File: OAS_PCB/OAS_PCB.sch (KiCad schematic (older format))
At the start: 57 parts, among them U1 TL072

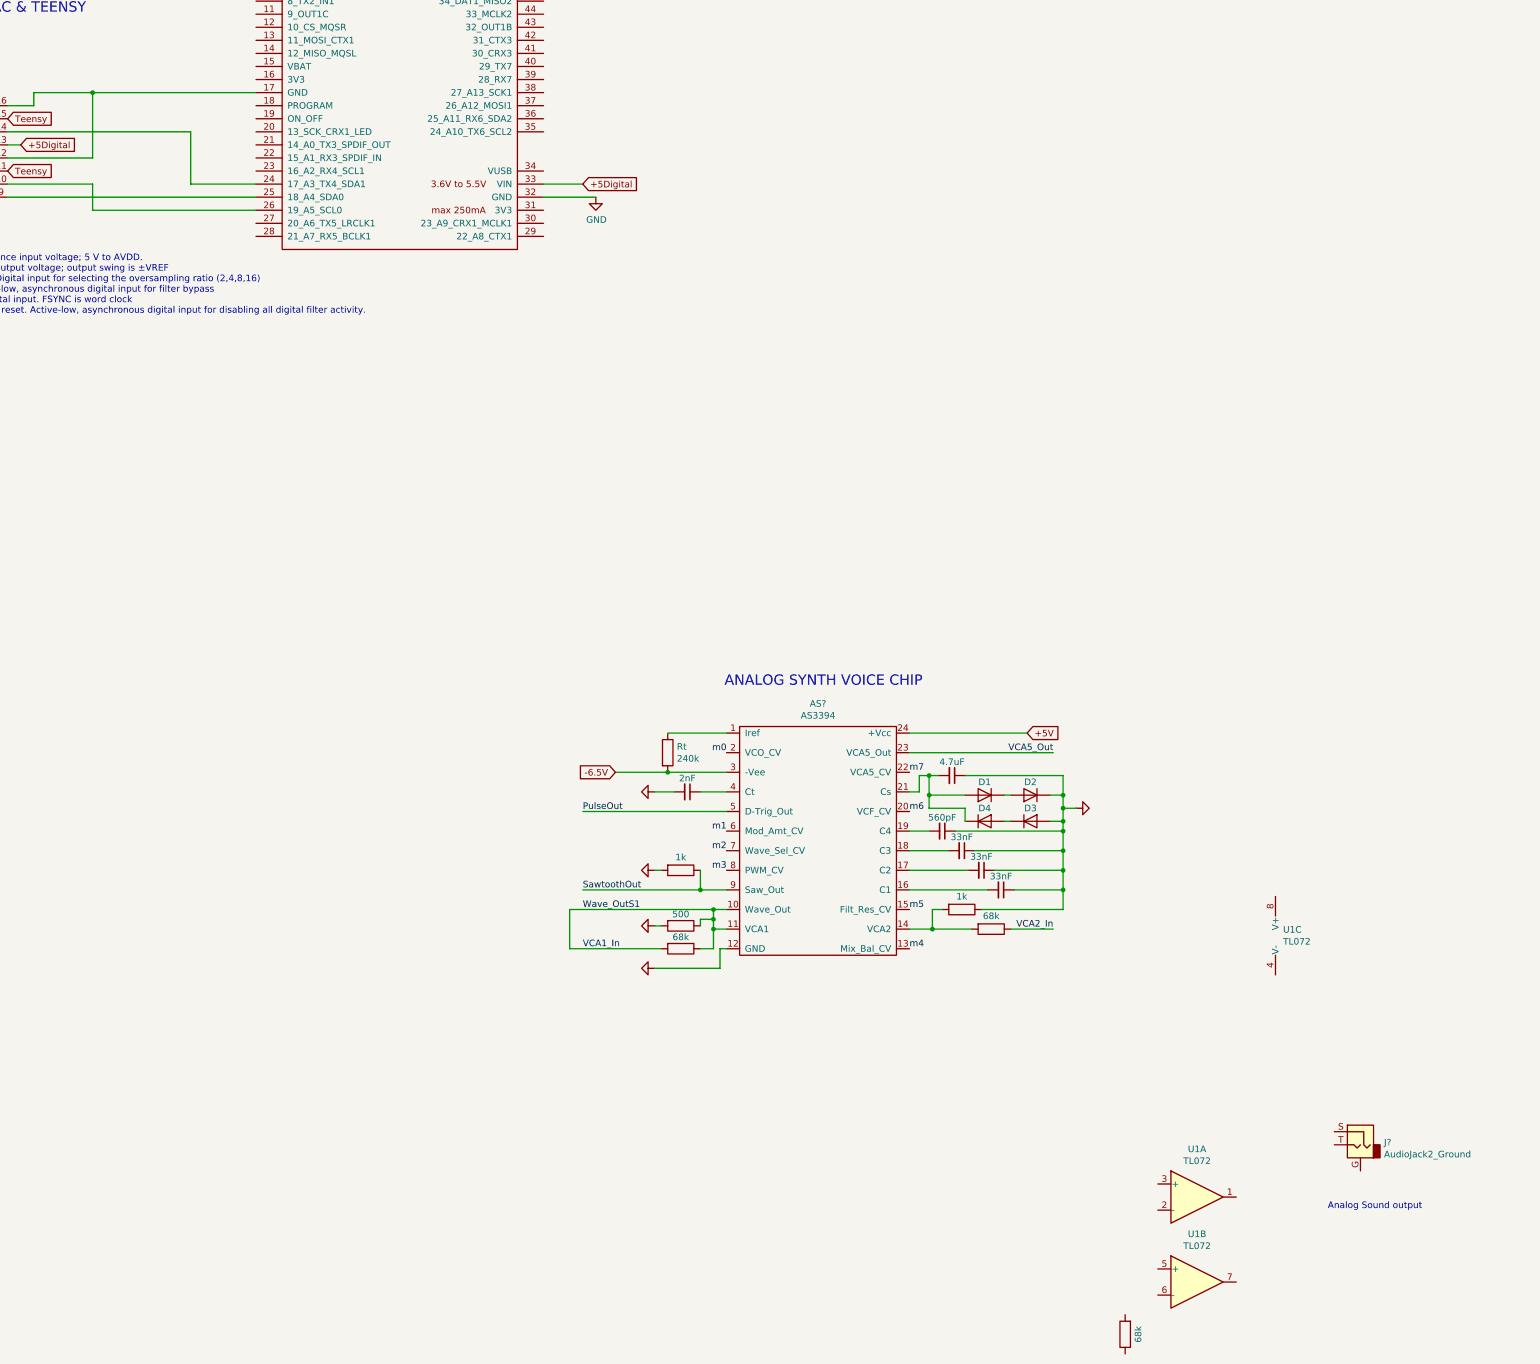
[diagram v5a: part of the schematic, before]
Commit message: Add analog output amplifier. connect waves to VCA1 & VCA2
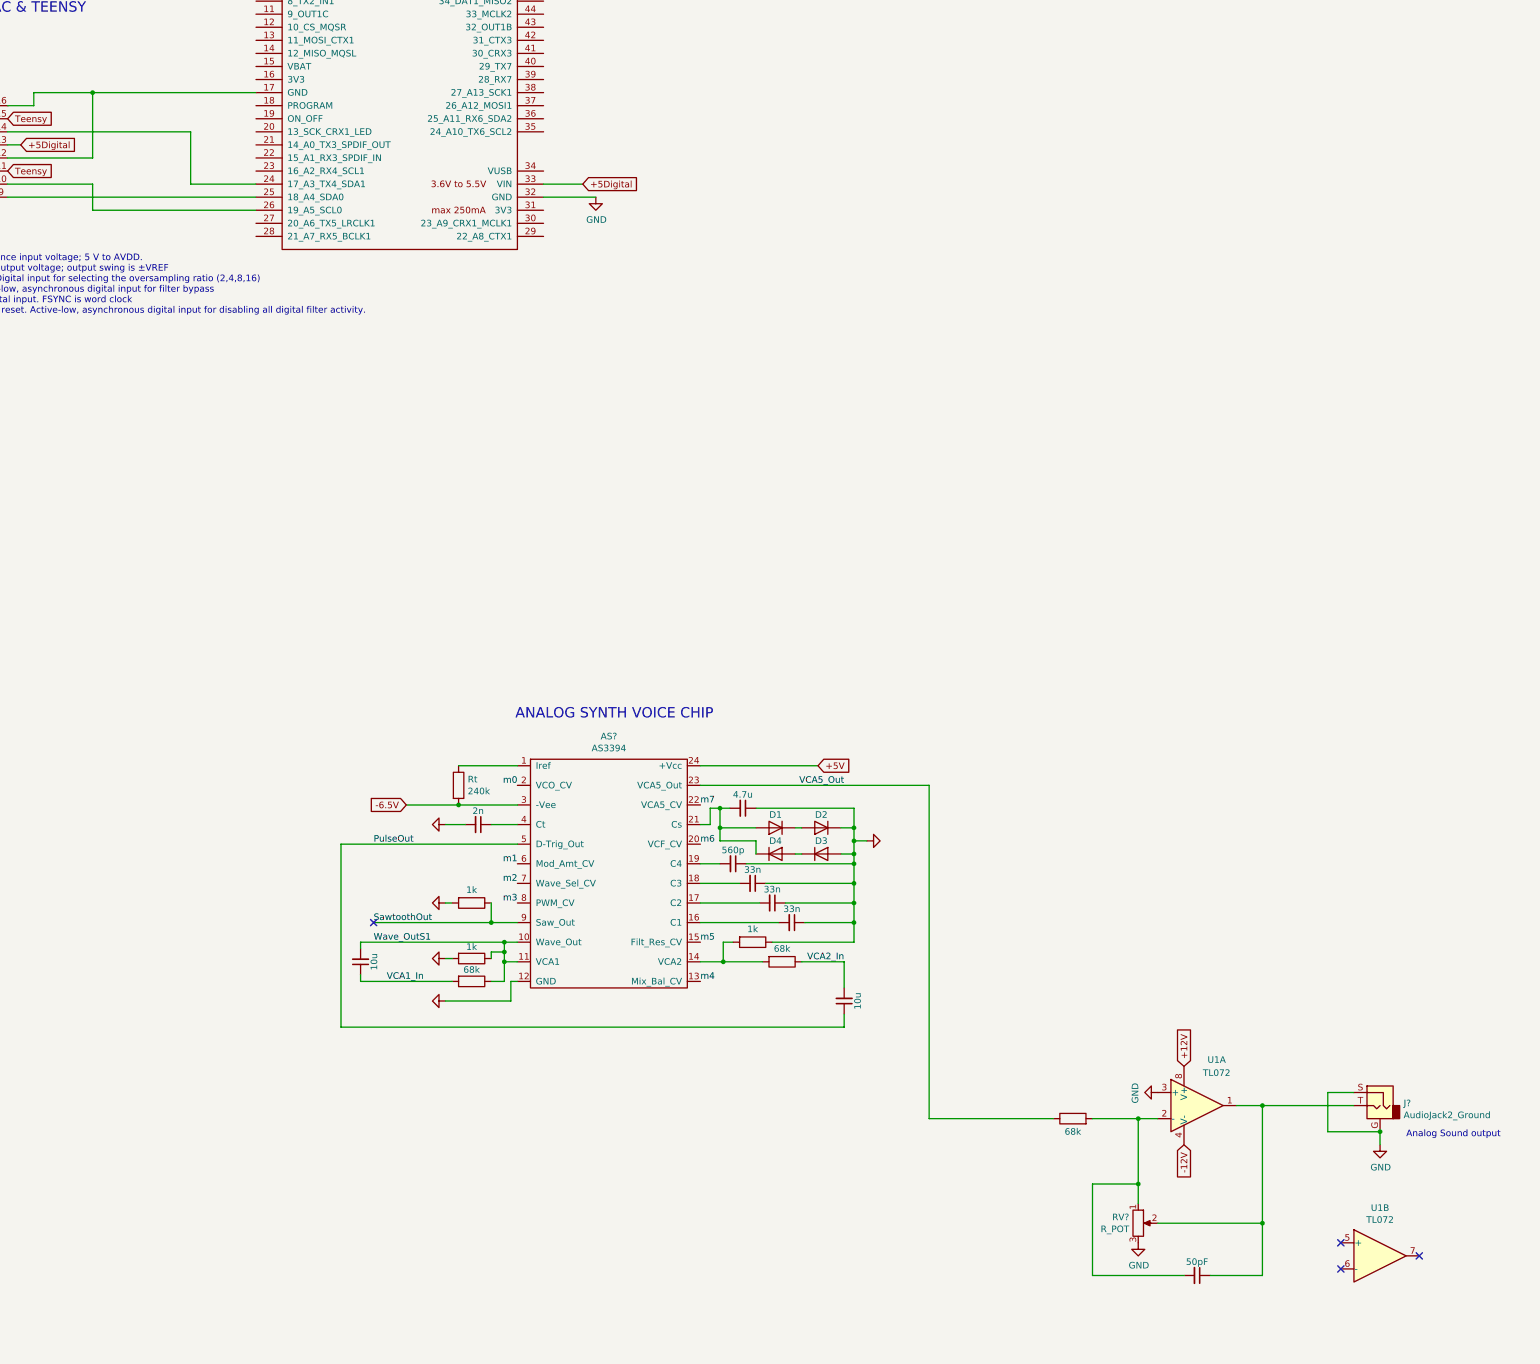
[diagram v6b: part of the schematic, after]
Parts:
- added C?: 50pF, symbol Device:C_Small
- added Cs? (x2): 10u, symbol Device:C_Small
- added RV?: R_POT, symbol Device:R_POT
- C1, C2, C3: value 33nF -> 33n
- C4: value 560pF -> 560p
- Cs: value 4.7uF -> 4.7u
- Ct: value 2nF -> 2n
- R?: value 500 -> 1k
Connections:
- net +12V: now also U1.8 (V+)
- net -12V: now also U1.4 (V-)
- net GND: now also J?.G, J?.S, U1.3 (+), RV?.3
- net PulseOut: now also Cs?.1
- net VCA1_In: now also Cs?.1; no longer AS?.10 (Wave_Out), AS?.11 (VCA1), R?.1, R?.1
- net VCA2_In: now also Cs?.2
- net VCA5_Out: now also R?.1
- net at J?.T: now also U1.1, C?.1, RV?.2
- net at U1.2 (-): now also R?.2, C?.2, RV?.1
- new net Wave_OutS1: AS?.10 (Wave_Out), AS?.11 (VCA1), Cs?.2, R?.1, R?.1
- no-connect marks 0 -> 4
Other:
- moved on the sheet: AS?, D1, D2, D3, D4, J?, Rt, U1A, U1B

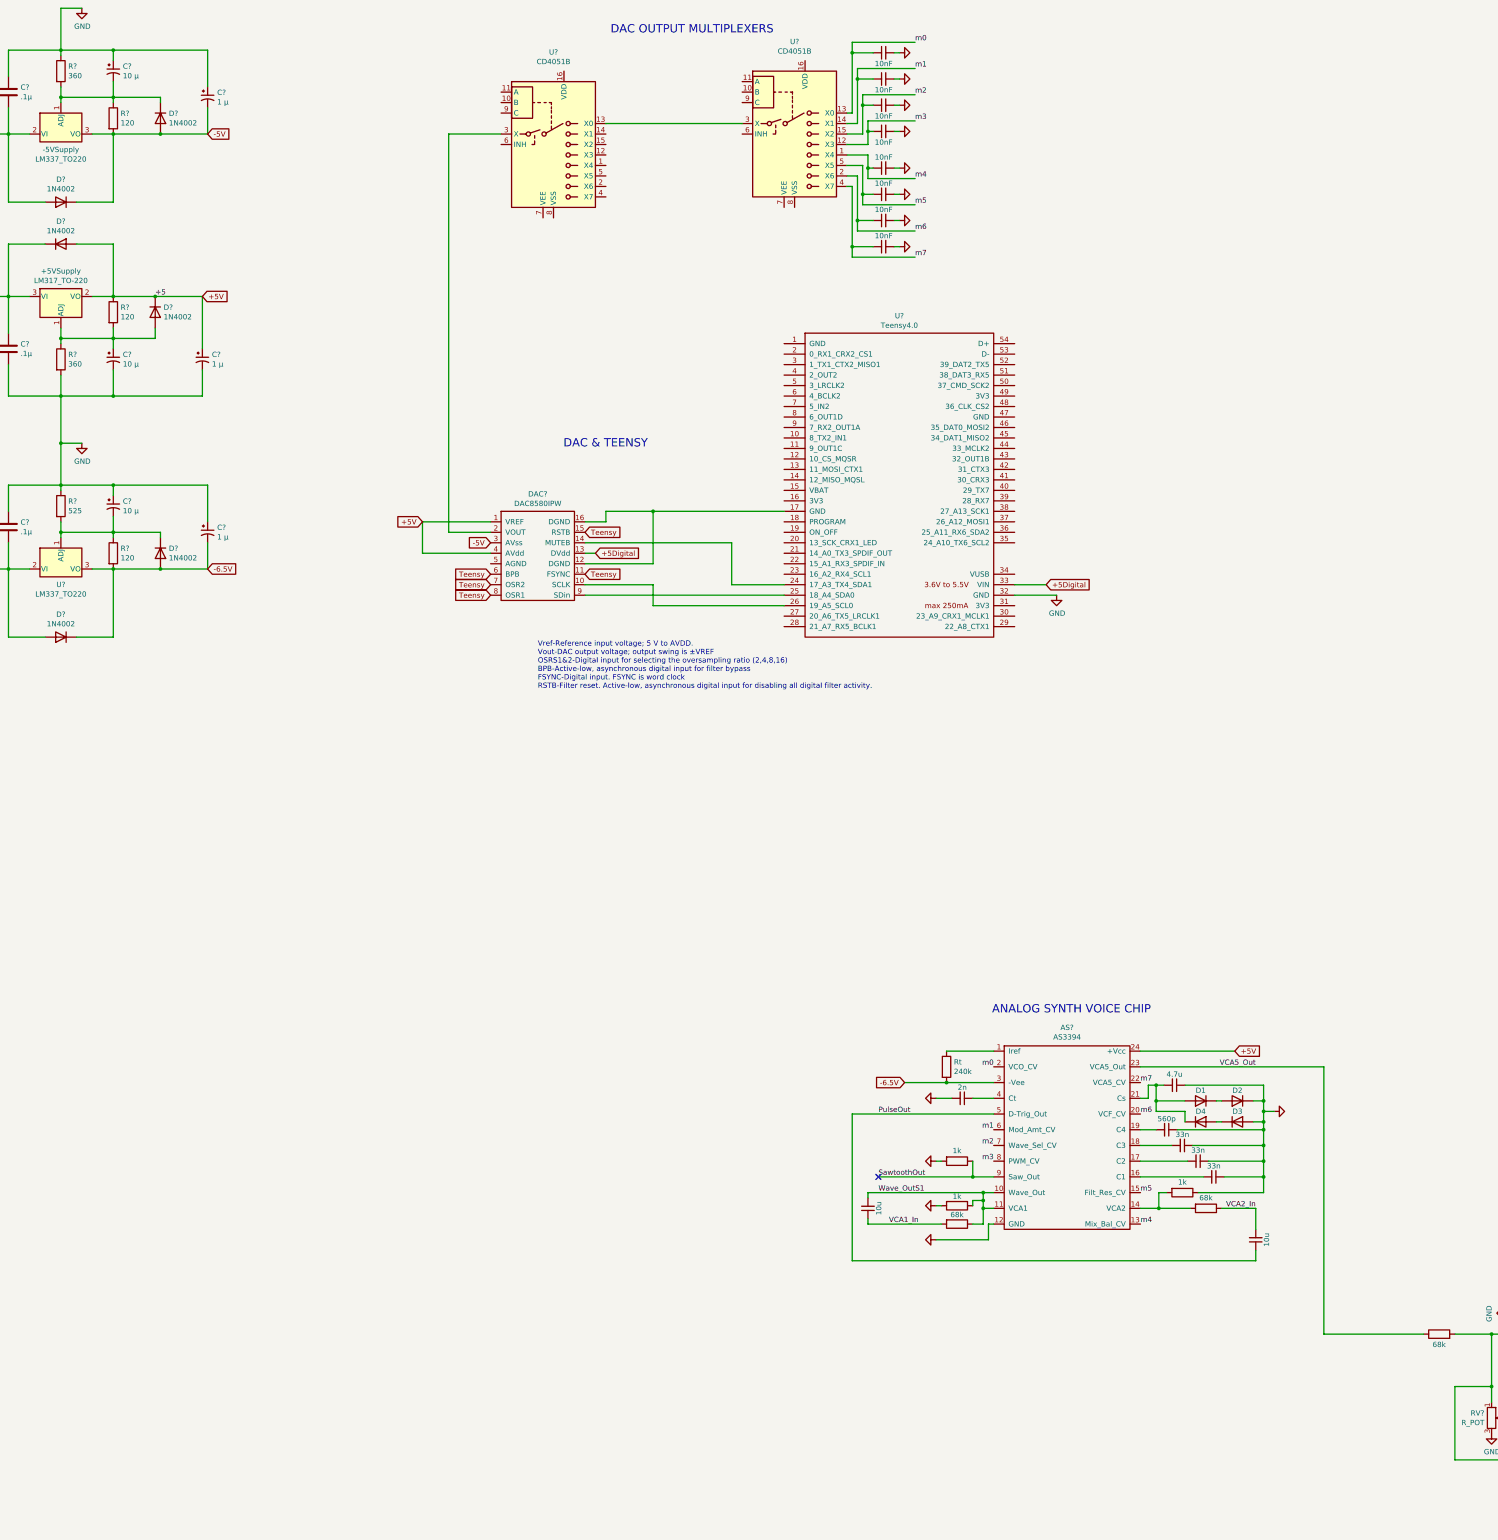
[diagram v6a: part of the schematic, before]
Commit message: duplicate AS3394 assembly, reconnect DAC to teensy audio pins
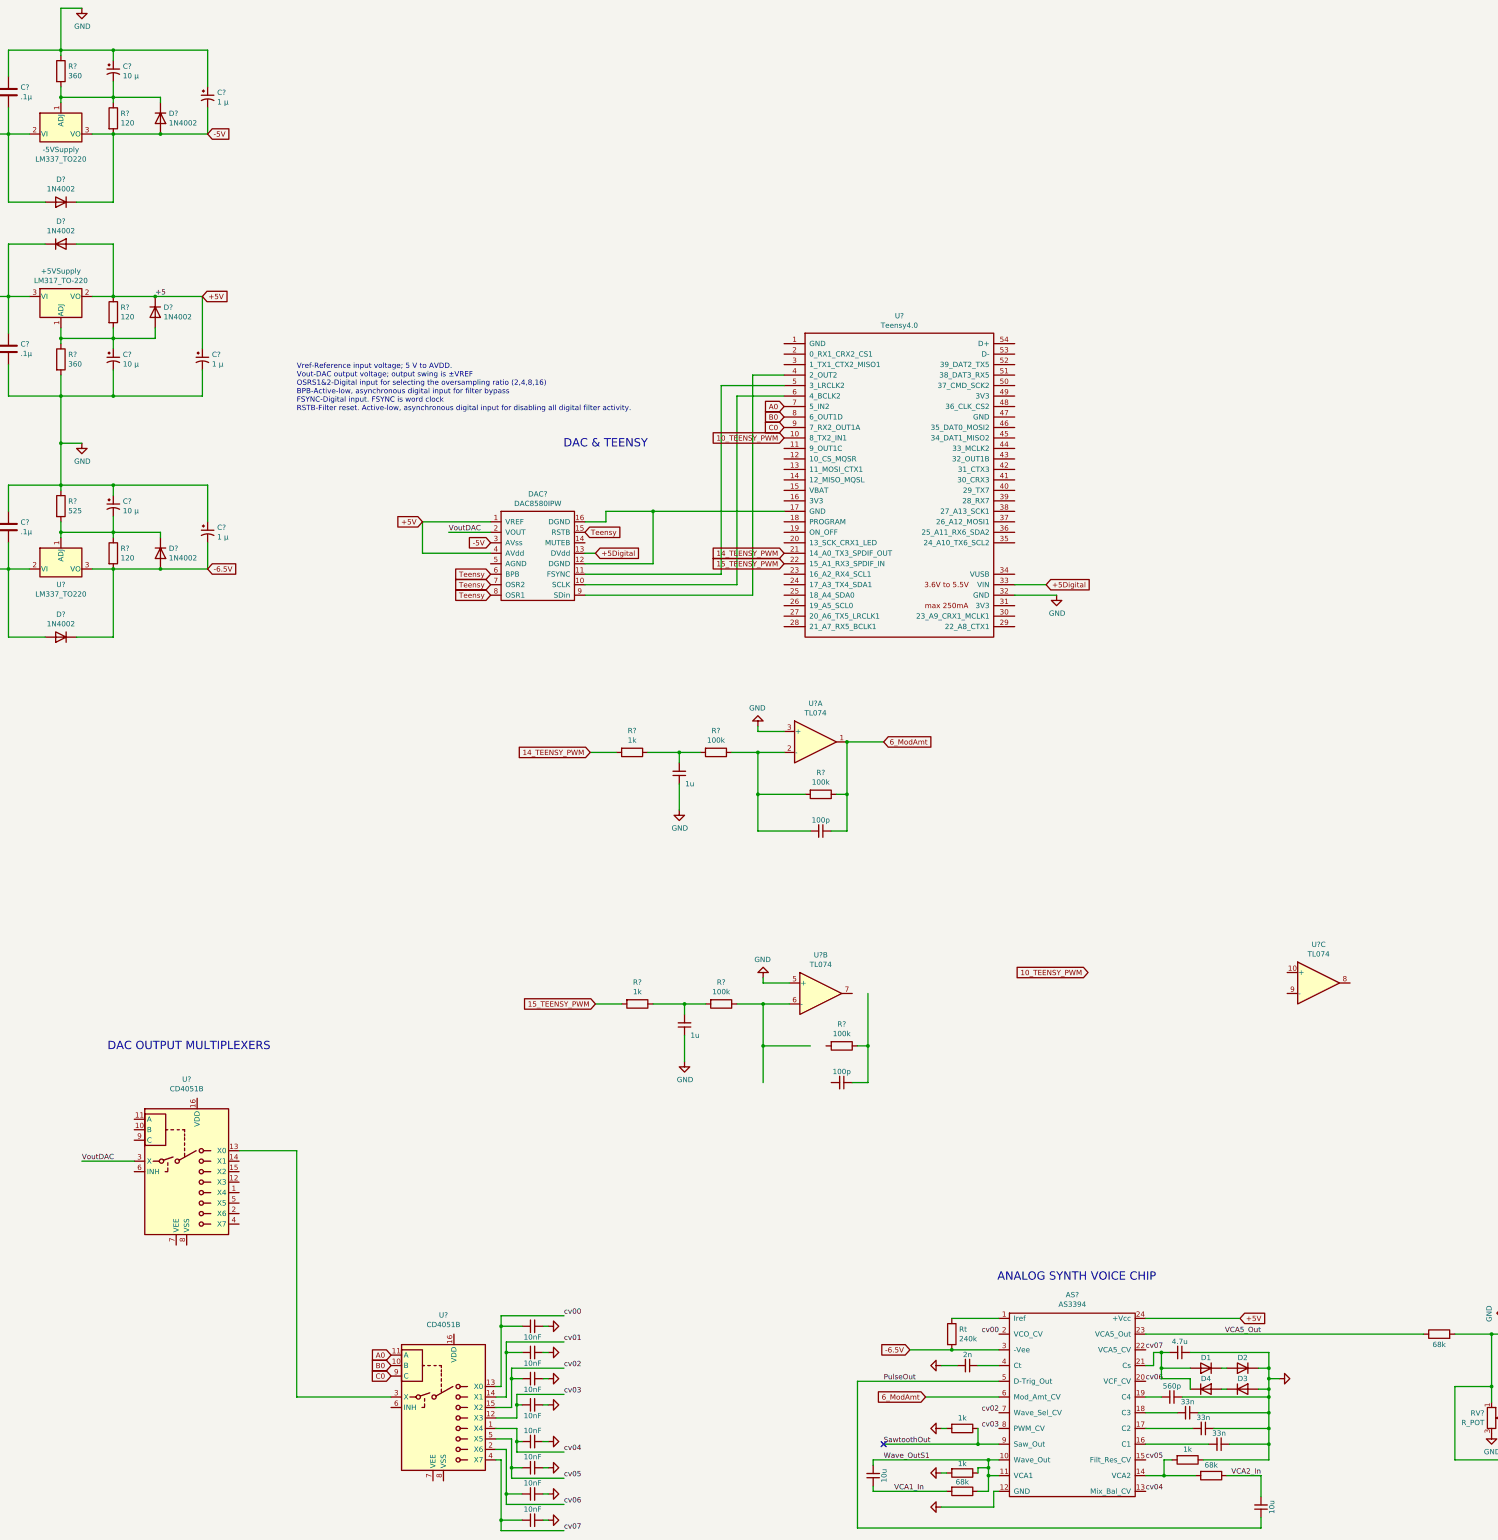
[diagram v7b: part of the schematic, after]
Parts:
- added Ct? (x2): 100p, symbol Device:C_Small
- added Ct? (x2): 1u, symbol Device:C_Small
- added R? (x4): 100k, symbol Device:R
- added R? (x2): 1k, symbol Device:R
- added U? (x3): TL074, symbol Amplifier_Operational:TL074
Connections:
- net GND: now also Ct?.1, Ct?.1, U?.3 (+), U?.5 (+)
- net Teensy: no longer DAC?.11 (FSYNC)
- net B0: now reaches U?.10 (B)
- net B0: now also U?.8 (6_OUT1D)
- net A0: now reaches U?.11 (A)
- net A0: now also U?.7 (5_IN2)
- net C0: now reaches U?.9 (C)
- net C0: now also U?.9 (7_RX2_OUT1A)
- net at DAC?.10 (SCLK): now also U?.6 (4_BCLK2); no longer U?.26 (19_A5_SCL0)
- net at DAC?.14 (MUTEB): no longer U?.24 (17_A3_TX4_SDA1)
- net VoutDAC: now reaches DAC?.2 (VOUT), U?.3 (X)
- net at DAC?.9 (SDin): now also U?.4 (2_OUT2); no longer U?.25 (18_A4_SDA0)
- net 10_TEENSY_PWM: now reaches U?.10 (8_TX2_IN1)
- net 14_TEENSY_PWM: now reaches U?.21 (14_A0_TX3_SPDIF_OUT)
- net 14_TEENSY_PWM: now also R?.2
- net 15_TEENSY_PWM: now reaches U?.22 (15_A1_RX3_SPDIF_IN)
- net 15_TEENSY_PWM: now also R?.2
- net at U?.5 (3_LRCLK2): now also DAC?.11 (FSYNC)
- net m0 renamed cv00
- net m1 renamed cv01
- net cv01: no longer AS?.6 (Mod_Amt_CV)
- net m2 renamed cv02
- net m3 renamed cv03
- net m4 renamed cv04
- net m5 renamed cv05
- net m6 renamed cv06
- net m7 renamed cv07
- new net: Ct?.2, R?.1, R?.2, U?.2 (-)
- new net: R?.1, U?.6 (-)
- new net: Ct?.2, R?.1, R?.2 (x2)
- new net: Ct?.1, R?.1
- new net 6_ModAmt: AS?.6 (Mod_Amt_CV), Ct?.1, R?.1, U?.1
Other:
- moved on the sheet: AS?, D1, D2, D3, D4, Rt, U?
